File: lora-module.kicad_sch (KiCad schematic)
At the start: 0 parts

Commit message: STM power mostly done
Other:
- sheet RF frontend ports: added RFI_N, RFI_P, RFO_LP, RF_ANT, RF_CTRL; removed none
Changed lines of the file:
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@@
       (effects (font (size 1.27 1.27)) (justify left))
+    )
+    (pin "RFI_P" output (at 157.48 93.98 180)
+      (effects (font (size 1.27 1.27)) (justify left))
+    )
+    (pin "RFO_LP" input (at 157.48 91.44 180)
+      (effects (font (size 1.27 1.27)) (justify left))
+    )
+    (pin "RFI_N" output (at 157.48 96.52 180)
+      (effects (font (size 1.27 1.27)) (justify left))
+    )
+    (pin "RF_CTRL" input (at 157.48 99.06 180)
+      (effects (font (size 1.27 1.27)) (justify left))
+    )
+    (pin "RF_ANT" bidirectional (at 184.15 93.98 0)
+      (effects (font (size 1.27 1.27)) (justify right))
     )
     (instances

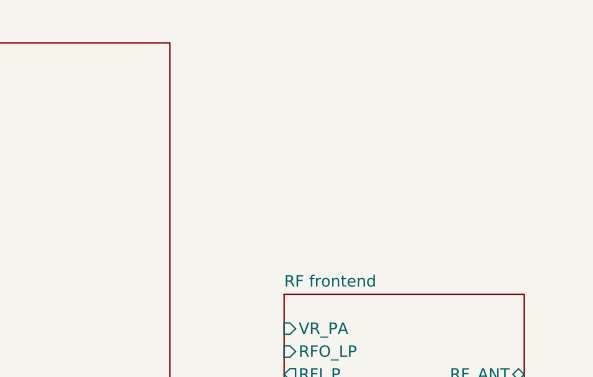
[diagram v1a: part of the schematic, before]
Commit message: added cubemx file for checking pinout
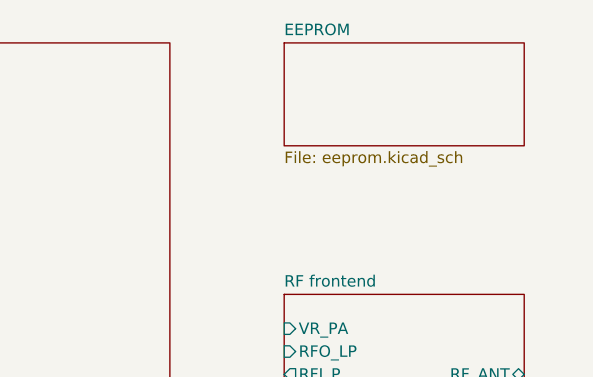
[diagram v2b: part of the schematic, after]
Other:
- added sheet EEPROM (eeprom.kicad_sch)
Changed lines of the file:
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@@
 (kicad_sch (version 20230121) (generator eeschema)
   (paper "A4")
+  (sheet (at 157.48 57.15) (size 26.67 11.43) (fields_autoplaced)
+    (stroke (width 0.1524) (type solid))
+    (fill (color 0 0 0 0.0000))
+    (property "Sheetname" "EEPROM" (at 157.48 56.4384 0)
+      (effects (font (size 1.27 1.27)) (justify left bottom))
+    )
+    (property "Sheetfile" "eeprom.kicad_sch" (at 157.48 69.1646 0)
+      (effects (font (size 1.27 1.27)) (justify left top))
+    )
+    (instances
+      (project "lora-module"
+        (path "/30c7e509-35af-4828-996b-9681d057624f" (page "4"))
+      )
+    )
+  )
   (sheet (at 157.48 85.09) (size 26.67 17.78) (fields_autoplaced)
     (stroke (width 0.1524) (type solid))

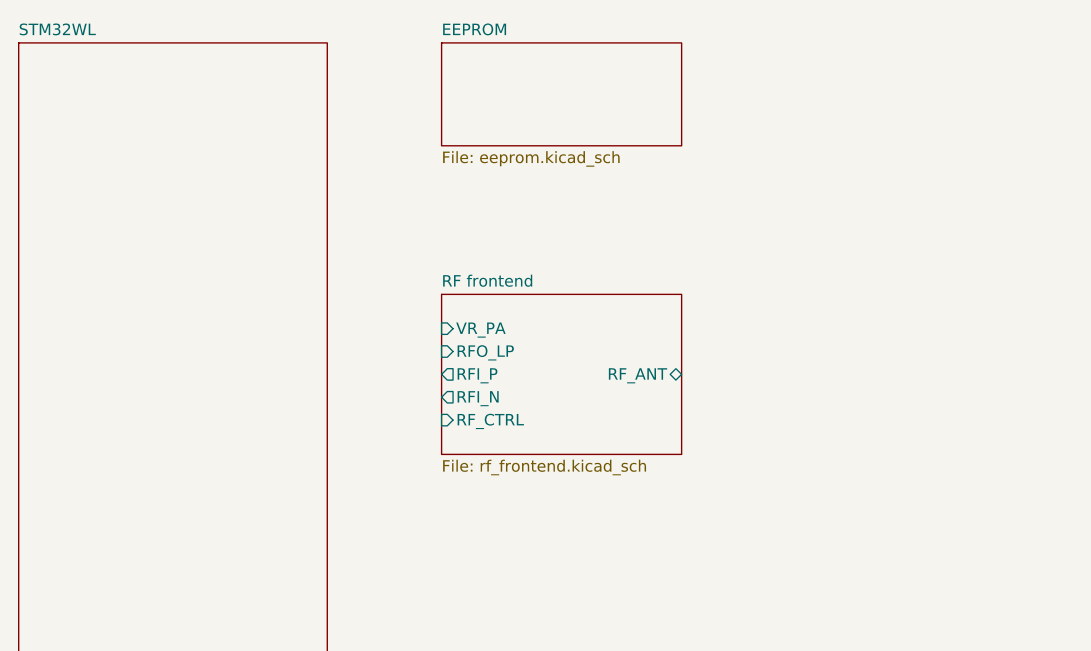
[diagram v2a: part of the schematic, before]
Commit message: most components placed, routed the RF section
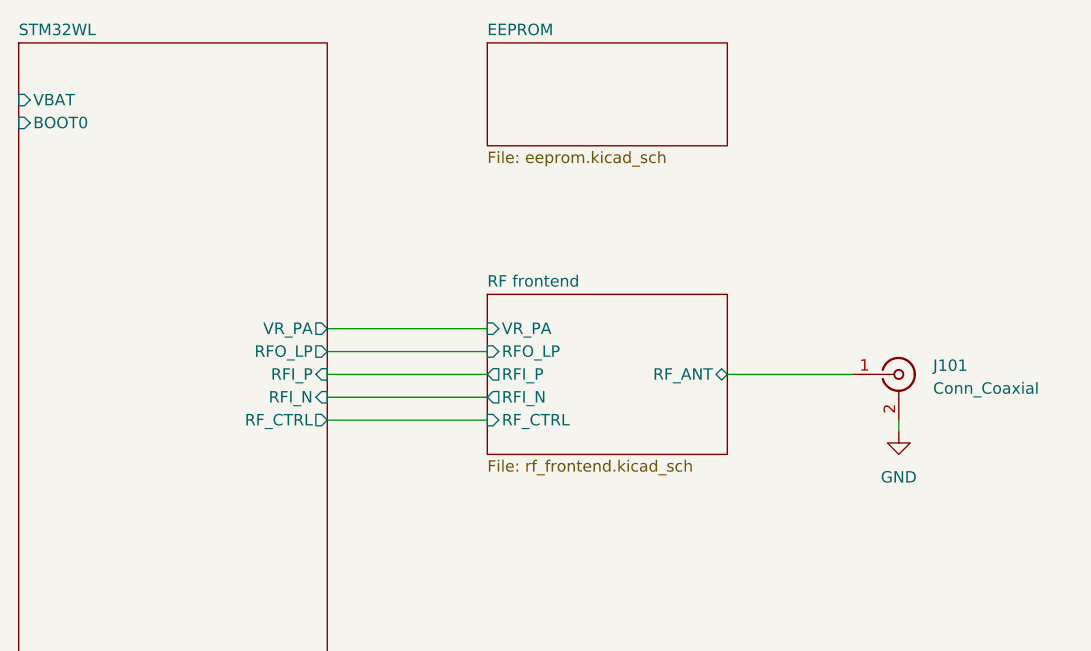
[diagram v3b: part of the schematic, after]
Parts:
- added J101: Conn_Coaxial, Connector_Coaxial:U.FL_Hirose_U.FL-R-SMT-1_Vertical, symbol Connector:Conn_Coaxial
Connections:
- net RF frontend/RF_ANT: now also J101.1 (In)
- new net GND: J101.2 (Ext)
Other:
- sheet STM32WL ports: added BOOT0, RFI_N, RFI_P, RFO_LP, RF_CTRL, VBAT, VR_PA; removed none
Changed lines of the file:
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@@
 (kicad_sch (version 20230121) (generator eeschema)
   (paper "A4")
-  (sheet (at 157.48 57.15) (size 26.67 11.43) (fields_autoplaced)
+  (wire (pts (xy 144.78 99.06) (xy 162.56 99.06))
+    (stroke (width 0) (type default))
+  )
+  (wire (pts (xy 208.28 99.06) (xy 208.28 100.33))
+    (stroke (width 0) (type default))
+  )
+  (wire (pts (xy 144.78 91.44) (xy 162.56 91.44))
+    (stroke (width 0) (type default))
+  )
+  (wire (pts (xy 189.23 93.98) (xy 203.2 93.98))
+    (stroke (width 0) (type default))
+  )
+  (wire (pts (xy 144.78 96.52) (xy 162.56 96.52))
+    (stroke (width 0) (type default))
+  )
+  (wire (pts (xy 144.78 93.98) (xy 162.56 93.98))
+    (stroke (width 0) (type default))
+  )
+  (wire (pts (xy 144.78 88.9) (xy 162.56 88.9))
+    (stroke (width 0) (type default))
+  )
+  (symbol (lib_id "power:GND") (at 208.28 100.33 0) (unit 1)
+    (in_bom yes) (on_board yes) (dnp no) (fields_autoplaced)
+    (property "Reference" "#PWR0101" (at 208.28 106.68 0)
+      (effects (font (size 1.27 1.27)) hide)
+    )
+    (property "Value" "GND" (at 208.28 105.41 0)
+      (effects (font (size 1.27 1.27)))
+    )
+    (property "Footprint" "" (at 208.28 100.33 0)
+      (effects (font (size 1.27 1.27)) hide)
+    )
+    (property "Datasheet" "" (at 208.28 100.33 0)
+      (effects (font (size 1.27 1.27)) hide)
+    )
+    (pin "1")
+    (instances
+      (project "lora-module"
+        (path "/30c7e509-35af-4828-996b-9681d057624f"
+          (reference "#PWR0101") (unit 1)
+        )
+      )
+    )
+  )
+  (symbol (lib_id "Connector:Conn_Coaxial") (at 208.28 93.98 0) (unit 1)
+    (in_bom yes) (on_board yes) (dnp no) (fields_autoplaced)
+    (property "Reference" "J101" (at 212.09 93.0032 0)
+      (effects (font (size 1.27 1.27)) (justify left))
+    )
+    (property "Value" "Conn_Coaxial" (at 212.09 95.5432 0)
+      (effects (font (size 1.27 1.27)) (justify left))
+    )
+    (property "Footprint" "Connector_Coaxial:U.FL_Hirose_U.FL-R-SMT-1_Vertical" (at 208.28 93.98 0)
+      (effects (font (size 1.27 1.27)) hide)
+    )
+    (property "Datasheet" " ~" (at 208.28 93.98 0)
+      (effects (font (size 1.27 1.27)) hide)
+    )
+    (pin "1")
+    (pin "2")
+    (instances
+      (project "lora-module"
+        (path "/30c7e509-35af-4828-996b-9681d057624f"
+          (reference "J101") (unit 1)
+        )
+      )
+    )
+  )
+  (sheet (at 162.56 57.15) (size 26.67 11.43) (fields_autoplaced)
     (stroke (width 0.1524) (type solid))
     (fill (color 0 0 0 0.0000))
-    (property "Sheetname" "EEPROM" (at 157.48 56.4384 0)
+    (property "Sheetname" "EEPROM" (at 162.56 56.4384 0)
       (effects (font (size 1.27 1.27)) (justify left bottom))
     )
-    (property "Sheetfile" "eeprom.kicad_sch" (at 157.48 69.1646 0)
+    (property "Sheetfile" "eeprom.kicad_sch" (at 162.56 69.1646 0)
       (effects (font (size 1.27 1.27)) (justify left top))
     )
@@
     )
   )
-  (sheet (at 157.48 85.09) (size 26.67 17.78) (fields_autoplaced)
+  (sheet (at 162.56 85.09) (size 26.67 17.78) (fields_autoplaced)
     (stroke (width 0.1524) (type solid))
     (fill (color 0 0 0 0.0000))
-    (property "Sheetname" "RF frontend" (at 157.48 84.3784 0)
+    (property "Sheetname" "RF frontend" (at 162.56 84.3784 0)
       (effects (font (size 1.27 1.27)) (justify left bottom))
     )
-    (property "Sheetfile" "rf_frontend.kicad_sch" (at 157.48 103.4546 0)
+    (property "Sheetfile" "rf_frontend.kicad_sch" (at 162.56 103.4546 0)
       (effects (font (size 1.27 1.27)) (justify left top))
     )
-    (pin "VR_PA" input (at 157.48 88.9 180)
+    (pin "VR_PA" input (at 162.56 88.9 180)
       (effects (font (size 1.27 1.27)) (justify left))
     )
-    (pin "RFI_P" output (at 157.48 93.98 180)
+    (pin "RFI_P" output (at 162.56 93.98 180)
       (effects (font (size 1.27 1.27)) (justify left))
     )
-    (pin "RFO_LP" input (at 157.48 91.44 180)
+    (pin "RFO_LP" input (at 162.56 91.44 180)
       (effects (font (size 1.27 1.27)) (justify left))
     )
-    (pin "RFI_N" output (at 157.48 96.52 180)
+    (pin "RFI_N" output (at 162.56 96.52 180)
       (effects (font (size 1.27 1.27)) (justify left))
     )
-    (pin "RF_CTRL" input (at 157.48 99.06 180)
+    (pin "RF_CTRL" input (at 162.56 99.06 180)
       (effects (font (size 1.27 1.27)) (justify left))
     )
-    (pin "RF_ANT" bidirectional (at 184.15 93.98 0)
+    (pin "RF_ANT" bidirectional (at 189.23 93.98 0)
       (effects (font (size 1.27 1.27)) (justify right))
     )
@@
       (effects (font (size 1.27 1.27)) hide)
     )
+    (pin "VBAT" input (at 110.49 63.5 180)
+      (effects (font (size 1.27 1.27)) (justify left))
+    )
+    (pin "RF_CTRL" output (at 144.78 99.06 0)
+      (effects (font (size 1.27 1.27)) (justify right))
+    )
+    (pin "RFO_LP" output (at 144.78 91.44 0)
+      (effects (font (size 1.27 1.27)) (justify right))
+    )
+    (pin "RFI_N" input (at 144.78 96.52 0)
+      (effects (font (size 1.27 1.27)) (justify right))
+    )
+    (pin "RFI_P" input (at 144.78 93.98 0)
+      (effects (font (size 1.27 1.27)) (justify right))
+    )
+    (pin "VR_PA" output (at 144.78 88.9 0)
+      (effects (font (size 1.27 1.27)) (justify right))
+    )
+    (pin "BOOT0" input (at 110.49 66.04 180)
+      (effects (font (size 1.27 1.27)) (justify left))
+    )
     (instances

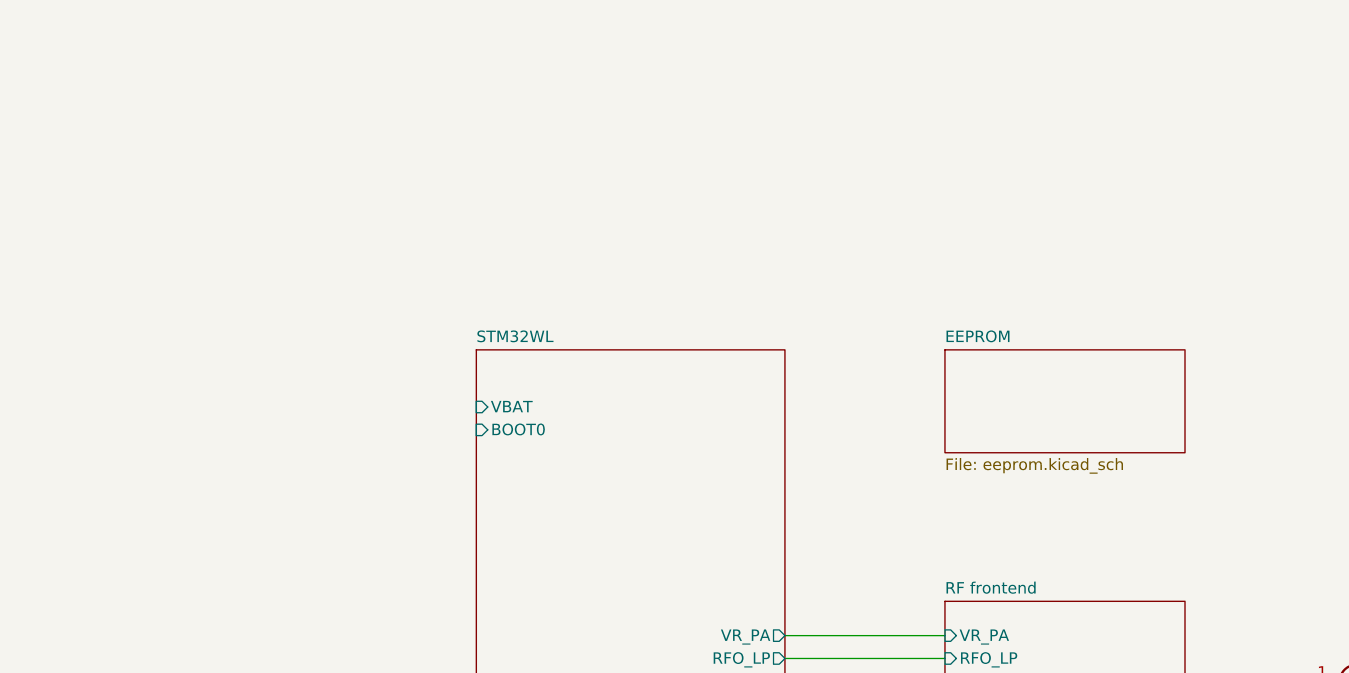
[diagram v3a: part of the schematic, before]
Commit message: most of the components are placed
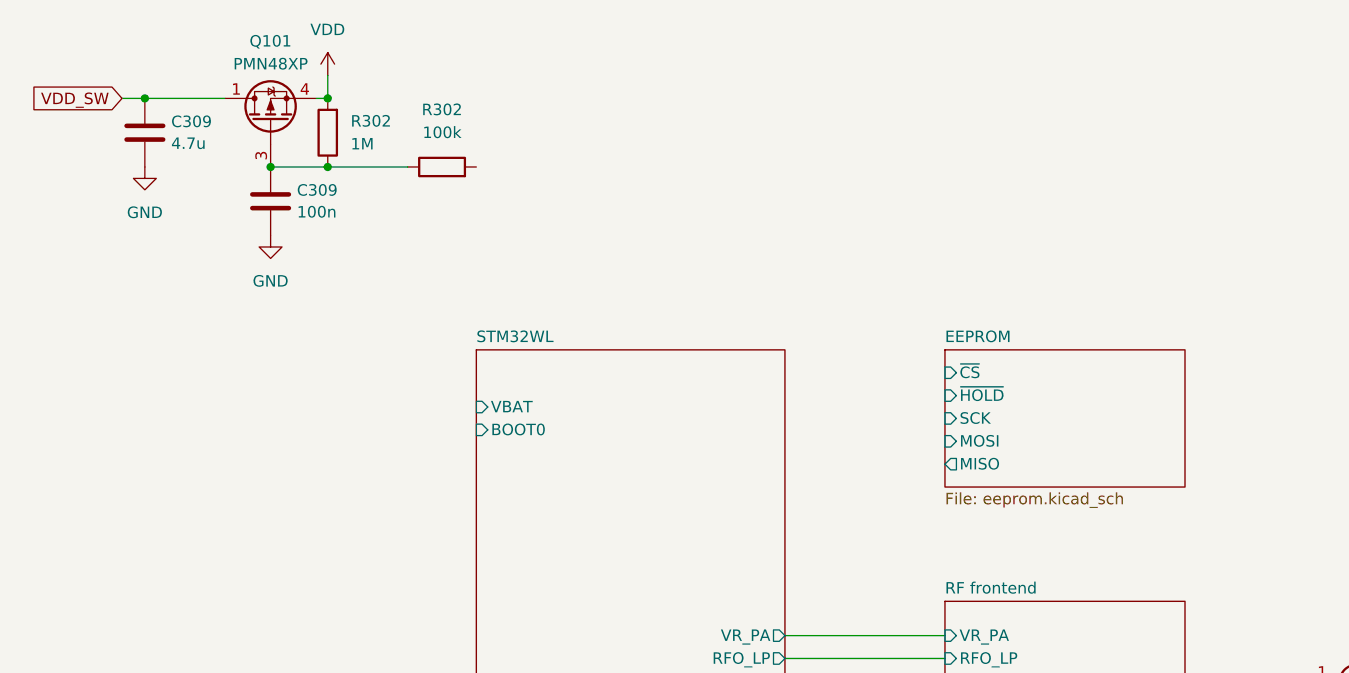
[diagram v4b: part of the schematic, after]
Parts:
- added C309: 4.7u, Capacitor_SMD:C_0603_1608Metric, symbol Device:C
- added C309: 100n, Capacitor_SMD:C_0402_1005Metric, symbol Device:C
- added Q101: PMN48XP, Package_SO:TSOP-6_1.65x3.05mm_P0.95mm, symbol Transistor_FET:PMN48XP
- added R302: 100k, Resistor_SMD:R_0402_1005Metric, symbol Device:R
- added R302: 1M, Resistor_SMD:R_0402_1005Metric, symbol Device:R
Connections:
- net GND: now also C309.2, C309.2
- new net: C309.1, Q101.3 (G), R302.1, R302.1
- new net VDD: Q101.4 (S), R302.2
- new net VDD_SW: C309.1, Q101.1 (D), Q101.2 (D), Q101.5 (D), Q101.6 (D)
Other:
- sheet EEPROM ports: added MISO, MOSI, SCK, ~{CS}, ~{HOLD}; removed none
